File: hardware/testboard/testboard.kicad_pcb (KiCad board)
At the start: 2 copper layers, 175 x 140 mm, 22 parts, among them J1 Reset, P1 Conn_01x06, P2 Conn_01x06, U1 68LC040, U10 SN74ALVC164245, U11 ICE40HX4K-TQ144, U13 SST26VF023BA, U14 SN74ALVC164245, U15 SN74ALVC164245, U2 MAX232, U3 MAX232, U4 68681, U6 IS61C5128AS-25TLI, U7 IS61C5128AS-25TLI, U8 NB3N502, X1 ASE-33MHz, X2 33MHz, X3 33MHz

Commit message: simpleboard nearly complete
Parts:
- removed P1, P2: Conn_01x06, 68040:15-48-0106
- removed RN1: 4.7k, Resistor_THT:R_Array_SIP6
- added C1: 0.22uF, Capacitor_SMD:C_0603_1608Metric, F.Cu at (146.1, 60.5)
- added C10: 1uF, Capacitor_SMD:C_0805_2012Metric, F.Cu at (54.2, 145.4)
- added C11: 1uF, Capacitor_SMD:C_0805_2012Metric, F.Cu at (61.2, 137.2)
- added C12: 1uF, Capacitor_SMD:C_0805_2012Metric, F.Cu at (53.7, 149.4)
- added C13: 1uF, Capacitor_SMD:C_0805_2012Metric, F.Cu at (60.6, 143.5)
- added C14: 1uF, Capacitor_SMD:C_0805_2012Metric, F.Cu at (54.2, 142.9)
- added C15: 15pF, Capacitor_SMD:C_0603_1608Metric, F.Cu at (62.9, 101.6)
- added C16: 15pF, Capacitor_SMD:C_0603_1608Metric, F.Cu at (62.9, 99.1)
- added C17: C_Polarized_Small_US, Capacitor_THT:CP_Radial_D5.0mm_P2.00mm, F.Cu at (78.7, 117.4)
- added C18: 100nF, Capacitor_SMD:C_0603_1608Metric, F.Cu at (56.8, 77.5)
- added C19: 100nF, Capacitor_SMD:C_0603_1608Metric, F.Cu at (132.4, 57.1)
- added C2: 22uF, Capacitor_THT:CP_Radial_D5.0mm_P2.00mm, F.Cu at (143.5, 81.3)
- added C21: 100nF, Capacitor_SMD:C_0603_1608Metric, F.Cu at (160.5, 114.3)
- added C22: 100nF, Capacitor_SMD:C_0603_1608Metric, F.Cu at (180.1, 114.3)
- added C23: 100nF, Capacitor_SMD:C_0603_1608Metric, F.Cu at (116.2, 46.4)
- added C24: 100nF, Capacitor_SMD:C_0603_1608Metric, F.Cu at (124.6, 47.7)
- added C25: 1uF, Capacitor_SMD:C_0805_2012Metric, F.Cu at (72.5, 137.9)
- added C26: 1uF, Capacitor_SMD:C_0805_2012Metric, F.Cu at (42.0, 148.9)
- added C27: 100nF, Capacitor_SMD:C_0603_1608Metric, F.Cu at (134.6, 131.3)
- added C28: 220uF, Capacitor_THT:CP_Radial_D8.0mm_P2.50mm, F.Cu at (43.2, 45.8)
- added C3: 220pF, Capacitor_SMD:C_0603_1608Metric, F.Cu at (183.7, 90.2)
- added C30: 100nF, Capacitor_SMD:C_0603_1608Metric, F.Cu at (100.2, 54.8)
- added C31: 100nF, Capacitor_SMD:C_0603_1608Metric, F.Cu at (85.8, 52.5)
- added C32: 100nF, Capacitor_SMD:C_0603_1608Metric, B.Cu at (122.3, 83.0)
- added C33: 100nF, Capacitor_SMD:C_0603_1608Metric, B.Cu at (122.3, 77.9)
- added C34: 100nF, Capacitor_SMD:C_0603_1608Metric, B.Cu at (116.3, 83.0)
- added C35: 100nF, Capacitor_SMD:C_0603_1608Metric, B.Cu at (116.3, 77.9)
- added C36: 100nF, Capacitor_SMD:C_0603_1608Metric, B.Cu at (75.6, 71.0)
- added C37: 100nF, Capacitor_SMD:C_0603_1608Metric, B.Cu at (75.6, 76.1)
- added C38: 100nF, Capacitor_SMD:C_0603_1608Metric, B.Cu at (69.5, 76.1)
- added C39: 100nF, Capacitor_SMD:C_0603_1608Metric, B.Cu at (69.5, 71.0)
- added C4: 0.22uF, Capacitor_SMD:C_0603_1608Metric, F.Cu at (196.8, 83.8)
- added C40: 100nF, Capacitor_SMD:C_0603_1608Metric, B.Cu at (101.4, 100.1)
- added C41: 100nF, Capacitor_SMD:C_0603_1608Metric, B.Cu at (80.0, 94.8)
- added C42: 100nF, Capacitor_SMD:C_0603_1608Metric, B.Cu at (86.4, 94.8)
- added C43: 100nF, Capacitor_SMD:C_0603_1608Metric, B.Cu at (106.4, 100.1)
- added C44: 100nF, Capacitor_SMD:C_0603_1608Metric, B.Cu at (101.4, 95.3)
- added C45: 100nF, Capacitor_SMD:C_0603_1608Metric, B.Cu at (80.0, 100.8)
- added C46: 100nF, Capacitor_SMD:C_0603_1608Metric, B.Cu at (106.4, 95.3)
- added C47: 100nF, Capacitor_SMD:C_0603_1608Metric, B.Cu at (86.4, 100.8)
- added C48: 100nF, Capacitor_SMD:C_0603_1608Metric, F.Cu at (83.6, 75.2)
- added C49: 100nF, Capacitor_SMD:C_0603_1608Metric, F.Cu at (110.4, 83.1)
- added C5: 22uF, Capacitor_THT:CP_Radial_D5.0mm_P2.00mm, F.Cu at (143.5, 48.3)
- added C50: 100nF, Capacitor_SMD:C_0603_1608Metric, F.Cu at (91.5, 90.4)
- added C51: 100nF, Capacitor_SMD:C_0603_1608Metric, B.Cu at (116.6, 100.1)
- added C52: 100nF, Capacitor_SMD:C_0603_1608Metric, B.Cu at (121.7, 100.1)
- added C53: 100nF, Capacitor_SMD:C_0603_1608Metric, B.Cu at (121.7, 95.3)
- added C54: 100nF, Capacitor_SMD:C_0603_1608Metric, B.Cu at (116.6, 95.3)
- added C55: 100nF, Capacitor_SMD:C_0603_1608Metric, F.Cu at (99.4, 63.3)
- added C56: 4.7uF, Capacitor_SMD:C_0603_1608Metric, F.Cu at (94.0, 90.7)
- added C57: 4.7uF, Capacitor_SMD:C_0603_1608Metric, F.Cu at (82.7, 78.1)
- added C58: 4.7uF, Capacitor_SMD:C_0603_1608Metric, F.Cu at (109.4, 86.4)
- added C59: 4.7uF, Capacitor_SMD:C_0603_1608Metric, F.Cu at (98.3, 61.6)
- added C6: 220pF, Capacitor_SMD:C_0603_1608Metric, F.Cu at (196.8, 44.0)
- added C60: 4.7uF, Capacitor_SMD:C_0603_1608Metric, F.Cu at (83.8, 65.4)
- added C61: 100nF, Capacitor_SMD:C_0603_1608Metric, F.Cu at (83.8, 63.5)
- added C62: 100nF, Capacitor_SMD:C_0603_1608Metric, F.Cu at (119.2, 67.0)
- added C63: 100nF, Capacitor_SMD:C_0603_1608Metric, F.Cu at (111.7, 58.4)
- added C64: 4.7uF, Capacitor_SMD:C_0603_1608Metric, F.Cu at (69.8, 57.9)
- added C65: 4.7uF, Capacitor_SMD:C_0603_1608Metric, F.Cu at (77.5, 57.9)
- added C66: 4.7uF, Capacitor_SMD:C_0603_1608Metric, B.Cu at (108.8, 70.1)
- added C67: 4.7uF, Capacitor_SMD:C_0603_1608Metric, B.Cu at (101.5, 70.1)
- added C68: 100nF, Capacitor_SMD:C_0603_1608Metric, B.Cu at (102.2, 73.8)
- added C69: 4.7uF, Capacitor_SMD:C_0603_1608Metric, B.Cu at (104.1, 75.1)
- added C7: 1uF, Capacitor_SMD:C_0805_2012Metric, F.Cu at (58.4, 138.1)
- added C70: 100nF, Capacitor_SMD:C_0603_1608Metric, B.Cu at (94.8, 68.6)
- added C71: 100nF, Capacitor_SMD:C_0603_1608Metric, B.Cu at (98.3, 83.2)
- added C72: 4.7uF, Capacitor_SMD:C_0603_1608Metric, B.Cu at (94.0, 75.7)
- added C73: 100nF, Capacitor_SMD:C_0603_1608Metric, F.Cu at (53.3, 36.3)
- added C74: 100nF, Capacitor_SMD:C_0603_1608Metric, F.Cu at (60.5, 57.1)
- added C75: 100nF, Capacitor_SMD:C_0603_1608Metric, F.Cu at (53.8, 57.1)
- added C8: 1uF, Capacitor_SMD:C_0805_2012Metric, F.Cu at (60.6, 141.0)
- added C9: 1uF, Capacitor_SMD:C_0805_2012Metric, F.Cu at (56.3, 148.4)
- added D1: LTST-C191KGKT, LED_SMD:LED_0603_1608Metric, F.Cu at (99.1, 41.4)
- added D2: D_Schottky, Diode_SMD:D_0603_1608Metric, F.Cu at (76.1, 41.4)
- added D3: LED, LED_THT:LED_D3.0mm, F.Cu at (32.5, 78.7)
- added FB1: FerriteBead, Inductor_SMD:L_0805_2012Metric_Pad1.15x1.40mm_HandSolder, F.Cu at (152.4, 37.1)
- added J2: Conn_01x06, Connector_JST:JST_PH_B6B-PH-K_1x06_P2.00mm_Vertical, F.Cu at (88.7, 35.6)
- added R1: 4.7k, Resistor_SMD:R_0603_1608Metric, F.Cu at (185.4, 37.3)
- added R10: 100, Resistor_SMD:R_0603_1608Metric, B.Cu at (94.8, 83.8)
- added R11: 4.7k, Resistor_SMD:R_0603_1608Metric, F.Cu at (180.3, 37.3)
- added R12: 4.7k, Resistor_SMD:R_0603_1608Metric, F.Cu at (177.8, 37.3)
- added R13: 4.7k, Resistor_SMD:R_0603_1608Metric, F.Cu at (175.3, 37.3)
- added R14: 10k, Resistor_SMD:R_0603_1608Metric, F.Cu at (94.2, 57.8)
- added R15: 2.2K, Resistor_SMD:R_0603_1608Metric, F.Cu at (38.7, 75.4)
- added R16: 2.2K, Resistor_SMD:R_0603_1608Metric, F.Cu at (100.3, 42.3)
- added R17: 10K, Resistor_SMD:R_0603_1608Metric, F.Cu at (81.1, 51.4)
- added R18: 10K, Resistor_SMD:R_0603_1608Metric, F.Cu at (89.6, 52.8)
- added R19: 10k, Resistor_SMD:R_0603_1608Metric, F.Cu at (94.2, 59.7)
- added R2: 1k, Resistor_SMD:R_0603_1608Metric, F.Cu at (62.2, 130.5)
- added R20: R_Small_US, Resistor_SMD:R_0603_1608Metric, F.Cu at (81.3, 85.5)
- added R21: 1k, Resistor_SMD:R_0603_1608Metric, F.Cu at (94.0, 121.9)
- added R22: 1k, Resistor_SMD:R_0603_1608Metric, F.Cu at (94.0, 120.7)
- added R23: 1k, Resistor_SMD:R_0603_1608Metric, F.Cu at (40.6, 67.8)
- added R24: 1k, Resistor_SMD:R_0603_1608Metric, F.Cu at (58.0, 47.0)
- added R25: 1k, Resistor_SMD:R_0603_1608Metric, F.Cu at (40.6, 59.2)
- added R26: 4.7k, Resistor_SMD:R_0603_1608Metric, F.Cu at (188.0, 37.3)
- added R27: 4.7k, Resistor_SMD:R_0603_1608Metric, F.Cu at (149.9, 37.3)
- added R28: 4.7k, Resistor_SMD:R_0603_1608Metric, F.Cu at (182.9, 37.3)
- added R29: 4.7k, Resistor_SMD:R_0603_1608Metric, F.Cu at (172.7, 37.3)
- added R3: 4.7k, Resistor_SMD:R_0603_1608Metric, F.Cu at (167.6, 37.3)
- added R4: 4.7k, Resistor_SMD:R_0603_1608Metric, F.Cu at (170.2, 37.3)
- added R5: 4.7k, Resistor_SMD:R_0603_1608Metric, F.Cu at (165.1, 37.3)
- added R6: 4.7k, Resistor_SMD:R_0603_1608Metric, F.Cu at (162.6, 37.3)
- added R7: 4.7k, Resistor_SMD:R_0603_1608Metric, F.Cu at (160.0, 37.3)
- added R8: 4.7k, Resistor_SMD:R_0603_1608Metric, F.Cu at (154.9, 37.3)
- added R9: 4.7k, Resistor_SMD:R_0603_1608Metric, F.Cu at (157.5, 37.3)
- added RN2: 1k, Resistor_THT:R_Array_SIP10, F.Cu at (141.0, 76.2)
- added SW1: Button, Button_Switch_THT:SW_PUSH_6mm, F.Cu at (30.5, 70.0)
- added SW2: Button, Button_Switch_THT:SW_PUSH_6mm, F.Cu at (30.5, 57.3)
- added U12: 74AHCT04, Package_SO:TSSOP-14_4.4x5mm_P0.65mm, F.Cu at (104.0, 55.4)
- added U16: SN74ALVC164245, Package_SO:TSSOP-48_6.1x12.5mm_P0.5mm, F.Cu at (83.2, 97.9)
- added U17: SN74ALVC164245, Package_SO:TSSOP-48_6.1x12.5mm_P0.5mm, F.Cu at (103.8, 97.7)
- added U18: SN74LVC07, Package_SO:TSSOP-14_4.4x5mm_P0.65mm, F.Cu at (115.4, 67.4)
- added U19: SN74LVC07, Package_SO:TSSOP-14_4.4x5mm_P0.65mm, F.Cu at (115.4, 58.5)
- added U20: AP2112K-3.3, Package_TO_SOT_SMD:SOT-23-5, F.Cu at (73.8, 58.1)
- added U21: AP2112K-1.2, Package_TO_SOT_SMD:SOT-23-5, B.Cu at (105.2, 70.2)
- added U22: 74LVC1G08, Package_TO_SOT_SMD:SOT-23-5, F.Cu at (56.8, 37.0)
- added U23: TL7705A, Package_SO:SOIC-8_3.9x4.9mm_P1.27mm, F.Cu at (57.8, 52.1)
- added U5: 74LVC1G04, Package_TO_SOT_SMD:SOT-23-5, F.Cu at (132.1, 61.0)
- added Y1: 3.6864MHz, Crystal:Crystal_C38-LF_D3.0mm_L8.0mm_Vertical, F.Cu at (67.5, 101.2)
- J1: value Reset -> Barrel_Jack; footprint Connector_PinHeader_2.54mm:PinHeader_1x02_P2.54mm_Vertical -> Connector_BarrelJack:BarrelJack_GCT_DCJ200-10-A_Horizontal
- U9: footprint Package_LCC:PLCC-68_SMD-Socket -> Package_LCC:PLCC-68_THT-Socket
- moved X2 87.6 mm to (111.8, 41.4), turned to 0 degrees
- moved X1 81.9 mm to (123.4, 37.1), turned to 0 degrees
- moved X3 80.4 mm to (119.4, 41.4), turned to 0 degrees
- moved U1 74.7 mm to (193.0, 86.4), turned to 180 degrees
- moved U4 68.7 mm to (43.2, 81.3), turned to 0 degrees
- moved U10 67.4 mm to (119.0, 97.3), turned to 90 degrees
- moved U7 67.1 mm to (180.6, 126.4), turned to 0 degrees
- moved U8 64.6 mm to (130.3, 47.2), turned to 0 degrees
- moved U15 59.0 mm to (72.5, 72.9), turned to 0 degrees
- moved U2 45.8 mm to (66.6, 141.6), turned to 0 degrees
- moved U9 41.0 mm to (127.0, 132.1), turned to -90 degrees
- moved J1 38.2 mm to (36.8, 37.5), turned to -90 degrees
- moved U6 36.1 mm to (160.5, 126.4), turned to 0 degrees
- moved U13 26.2 mm to (86.2, 56.9), turned to 0 degrees
- moved U11 24.7 mm to (96.3, 76.1), turned to 180 degrees
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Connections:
- J1 pad 1: unconnected-(J1-Pin_1-Pad1) -> +5V
- U1 pad R16: /~{TS} -> Net-(U1A-~{TS})
- U1 pad R3: /CPU/~{SW_RST} -> /~{SW_RST}
- U1 pad S11: /~{TCI}/~{TBI} -> /~{TBI}
- U1 pad S7: /CPU/~{HW_RST} -> /~{RST}
- U1 pad T10: /~{TCI}/~{TBI} -> /~{TCI}
- U10 pad 1: /FPGA/FPGA_D_DIR -> GND
- U10 pad 11: /PD30 -> GND
- U10 pad 12: /PD31 -> GND
- U10 pad 13: /PA0 -> /SIZ0
- U10 pad 14: /PA1 -> /SIZ1
- U10 pad 16: unconnected-(U10A-2B3-Pad16) -> /~{COM_IRQ}
- U10 pad 17: unconnected-(U10A-2B4-Pad17) -> /~{RST}
- U10 pad 19: unconnected-(U10A-2B5-Pad19) -> /~{TS}
- U10 pad 2: /PD24 -> /TT0
- U10 pad 20: unconnected-(U10A-2B6-Pad20) -> /~{TIP}
- U10 pad 22: /FPGA/~{68150_DS} -> /~{DS}
- U10 pad 23: unconnected-(U10A-2B8-Pad23) -> /R/~{W}
- U10 pad 26: unconnected-(U10A-2A8-Pad26) -> /FPGA/LV_R/~{W}
- U10 pad 29: unconnected-(U10A-2A6-Pad29) -> /FPGA/LV_~{TIP}
- U10 pad 3: /PD25 -> /TT1
- U10 pad 30: unconnected-(U10A-2A5-Pad30) -> /FPGA/LV_~{TS}
- U10 pad 32: unconnected-(U10A-2A4-Pad32) -> /FPGA/LV_~{RST}
- U10 pad 33: unconnected-(U10A-2A3-Pad33) -> /FPGA/LV_~{COM_IRQ}
- U10 pad 35: /FPGA/LV_PA1 -> /FPGA/LV_SIZ1
- U10 pad 36: /FPGA/LV_PA0 -> /FPGA/LV_SIZ0
- U10 pad 37: /FPGA/FPGA_D7 -> unconnected-(U10A-1A8-Pad37)
- U10 pad 38: /FPGA/FPGA_D6 -> unconnected-(U10A-1A7-Pad38)
- U10 pad 40: /FPGA/FPGA_D5 -> unconnected-(U10A-1A6-Pad40)
- U10 pad 41: /FPGA/FPGA_D4 -> /FPGA/LV_TM2
- U10 pad 43: /FPGA/FPGA_D3 -> /FPGA/LV_TM1
- U10 pad 44: /FPGA/FPGA_D2 -> /FPGA/LV_TM0
- U10 pad 46: /FPGA/FPGA_D1 -> /FPGA/LV_TT1
- U10 pad 47: /FPGA/FPGA_D0 -> /FPGA/LV_TT0
- U10 pad 48: /FPGA/FPGA_D_~{OE} -> GND
- U10 pad 5: /PD26 -> /TM0
- U10 pad 6: /PD27 -> /TM1
- U10 pad 8: /PD28 -> /TM2
- U10 pad 9: /PD29 -> GND
- U11 pad 1: /FPGA/~{DSACK0} -> /FPGA/LV.A0
- U11 pad 10: unconnected-(U11D-IOL_5B-Pad10) -> /FPGA/LV.A7
- U11 pad 101: /FPGA/LV.A23 -> /FPGA/LV_D7
- U11 pad 102: /FPGA/LV.A24 -> /FPGA/LV_D8
- U11 pad 104: /FPGA/LV.A25 -> /FPGA/LV_D9
- U11 pad 105: /FPGA/LV.A26 -> /FPGA/LV_D10
- U11 pad 106: /FPGA/LV.A27 -> /FPGA/LV_D11
- U11 pad 107: /FPGA/LV.A28 -> /FPGA/LV_D12
- U11 pad 109: +3.3V -> unconnected-(U11E-VPP_FAST-Pad109)
- U11 pad 11: unconnected-(U11D-IOL_8A-Pad11) -> /FPGA/LV.A8
- U11 pad 110: /FPGA/LV.A29 -> /FPGA/LV_D13
- U11 pad 111: +3.3V -> +1V2
- U11 pad 112: /FPGA/LV.A30 -> /FPGA/LV_D14
- U11 pad 113: /FPGA/LV.A31 -> /FPGA/LV_D15
- U11 pad 114: /FPGA/FPGA_D0 -> /FPGA/LV_D16
- U11 pad 115: /FPGA/FPGA_D1 -> /FPGA/LV_D17
- U11 pad 116: /FPGA/FPGA_D2 -> /FPGA/LV_D18
- U11 pad 117: /FPGA/FPGA_D3 -> /FPGA/LV_D19
- U11 pad 118: /FPGA/FPGA_D4 -> /FPGA/LV_D20
- U11 pad 119: /FPGA/FPGA_D5 -> /FPGA/LV_D21
- U11 pad 12: unconnected-(U11D-IOL_8B-Pad12) -> /FPGA/LV.A9
- U11 pad 120: /FPGA/FPGA_D6 -> /FPGA/LV_D22
- U11 pad 121: /FPGA/FPGA_D7 -> /FPGA/LV_D23
- U11 pad 122: unconnected-(U11A-IOT_190-Pad122) -> /FPGA/LV_D24
- U11 pad 124: unconnected-(U11A-IOT_191-Pad124) -> /FPGA/LV_D25
- U11 pad 125: unconnected-(U11A-IOT_192-Pad125) -> /FPGA/LV_D26
- U11 pad 126: +3.3V -> /FPGA/VCC_PLL
- U11 pad 127: GND -> /FPGA/GND_PLL
- U11 pad 128: unconnected-(U11A-IOT_197_GBIN1-Pad128) -> /FPGA/LV_D27
- U11 pad 129: unconnected-(U11A-IOT_198_GBIN0-Pad129) -> /FPGA/LV_D28
- U11 pad 130: unconnected-(U11A-IOT_206-Pad130) -> /FPGA/LV_D29
- U11 pad 134: unconnected-(U11A-IOT_212-Pad134) -> /FPGA/LV_D30
- U11 pad 135: unconnected-(U11A-IOT_213-Pad135) -> /FPGA/LV_D31
- U11 pad 136: unconnected-(U11A-IOT_214-Pad136) -> /FPGA/LV_TT0
- U11 pad 137: unconnected-(U11A-IOT_215-Pad137) -> /FPGA/LV_TT1
- U11 pad 138: unconnected-(U11A-IOT_216-Pad138) -> /FPGA/LV_SIZ0
- U11 pad 139: unconnected-(U11A-IOT_217-Pad139) -> /FPGA/LV_SIZ1
- U11 pad 141: unconnected-(U11A-IOT_219-Pad141) -> /FPGA/LV_~{TS}
- U11 pad 142: unconnected-(U11A-IOT_220-Pad142) -> /FPGA/LV_~{TIP}
- U11 pad 143: unconnected-(U11A-IOT_221-Pad143) -> /FPGA/LV_~{68150_DS}
- U11 pad 144: unconnected-(U11A-IOT_222-Pad144) -> /FPGA/LV_R/~{W}
- U11 pad 15: unconnected-(U11D-IOL_10A-Pad15) -> /FPGA/LV.A10
- U11 pad 16: unconnected-(U11D-IOL_10B-Pad16) -> /FPGA/LV.A11
- U11 pad 17: unconnected-(U11D-IOL_12A-Pad17) -> /FPGA/LV.A12
- U11 pad 18: unconnected-(U11D-IOL_12B-Pad18) -> /FPGA/LV.A13
- U11 pad 19: unconnected-(U11D-IOL_13A-Pad19) -> /FPGA/LV.A14
- U11 pad 2: /FPGA/~{DSACK1} -> /FPGA/LV.A1
- U11 pad 20: unconnected-(U11D-IOL_13B_GBIN7-Pad20) -> /FPGA/LV.A15
- U11 pad 21: unconnected-(U11D-IOL_14A_GBIN6-Pad21) -> /FPGA/LV_~{DSACK0}
- U11 pad 22: unconnected-(U11D-IOL_14B-Pad22) -> /FPGA/LV_~{DSACK1}
- U11 pad 23: unconnected-(U11D-IOL_17A-Pad23) -> /FPGA/LV_TM0
- U11 pad 24: unconnected-(U11D-IOL_17B-Pad24) -> /FPGA/LV_TM1
- U11 pad 25: unconnected-(U11D-IOL_18A-Pad25) -> /FPGA/LV_TM2
- U11 pad 26: unconnected-(U11D-IOL_18B-Pad26) -> /FPGA/LV_~{TA}
- U11 pad 27: +3.3V -> +1V2
- U11 pad 28: unconnected-(U11D-IOL_23A-Pad28) -> /FPGA/LV_~{TEA}
- U11 pad 29: unconnected-(U11D-IOL_23B-Pad29) -> /FPGA/LV_~{TBI}
- U11 pad 3: unconnected-(U11D-IOL_3A-Pad3) -> /FPGA/LV.A2
- U11 pad 31: unconnected-(U11D-IOL_24A-Pad31) -> /FPGA/LV_~{TCI}
- U11 pad 32: unconnected-(U11D-IOL_24B-Pad32) -> /FPGA/LV_~{IPL0}
- U11 pad 33: unconnected-(U11D-IOL_25A-Pad33) -> /FPGA/LV_~{IPL1}
- U11 pad 34: unconnected-(U11D-IOL_25B-Pad34) -> /FPGA/LV_~{IPL2}
- U11 pad 4: unconnected-(U11D-IOL_3B-Pad4) -> /FPGA/LV.A3
- U11 pad 40: +3.3V -> +1V2
- U11 pad 41: unconnected-(U11C-IOB_63-Pad41) -> /FPGA/LV_RAM_CS
- U11 pad 42: unconnected-(U11C-IOB_64-Pad42) -> /FPGA/LV_COM_IACK
- U11 pad 43: unconnected-(U11C-IOB_71-Pad43) -> /FPGA/LV_~{COM_IRQ}
- U11 pad 44: unconnected-(U11C-IOB_72-Pad44) -> /FPGA/LV_COM_CS
- U11 pad 45: unconnected-(U11C-IOB_73-Pad45) -> /FPGA/LV_68150_CS
- U11 pad 47: unconnected-(U11C-IOB_79-Pad47) -> /FPGA/FPGA_D_~{OE}
- U11 pad 48: unconnected-(U11C-IOB_80-Pad48) -> /FPGA/FPGA_D_DIR
- U11 pad 49: unconnected-(U11C-IOB_81_GBIN5-Pad49) -> /FPGA/LV_~{RST}
- U11 pad 53: GND -> /FPGA/GND_PLL
- U11 pad 54: +3.3V -> /FPGA/VCC_PLL
- U11 pad 55: /FPGA/FPGA_A_DIR -> /FPGA/FPGA_LED
- U11 pad 56: /FPGA/FPGA_A_~{OE} -> /FPGA/FPGA_BTN
- U11 pad 66: unconnected-(U11E-~{CRESET}-Pad66) -> Net-(U11E-~{CRESET})
- U11 pad 7: unconnected-(U11D-IOL_4A-Pad7) -> /FPGA/LV.A4
- U11 pad 73: /FPGA/LV.A0 -> /FPGA/LV.A16
- U11 pad 74: /FPGA/LV.A1 -> /FPGA/LV.A17
- U11 pad 75: /FPGA/LV.A2 -> /FPGA/LV.A18
- U11 pad 76: /FPGA/LV.A3 -> /FPGA/LV.A19
- U11 pad 78: /FPGA/LV.A4 -> /FPGA/LV.A20
- U11 pad 79: /FPGA/LV.A5 -> /FPGA/LV.A21
- U11 pad 8: unconnected-(U11D-IOL_4B-Pad8) -> /FPGA/LV.A5
- U11 pad 80: /FPGA/LV.A6 -> /FPGA/LV.A22
- U11 pad 81: /FPGA/LV.A7 -> /FPGA/LV.A23
- U11 pad 82: /FPGA/LV.A8 -> /FPGA/LV.A24
- U11 pad 83: /FPGA/LV.A9 -> /FPGA/LV.A25
- U11 pad 84: /FPGA/LV.A10 -> /FPGA/LV.A26
- U11 pad 85: /FPGA/LV.A11 -> /FPGA/LV.A27
- U11 pad 87: /FPGA/LV.A12 -> /FPGA/LV.A28
- U11 pad 88: /FPGA/LV.A13 -> /FPGA/LV.A29
- U11 pad 9: unconnected-(U11D-IOL_5A-Pad9) -> /FPGA/LV.A6
- U11 pad 90: /FPGA/LV.A14 -> /FPGA/LV.A30
- U11 pad 91: /FPGA/LV.A15 -> /FPGA/LV.A31
- U11 pad 92: +3.3V -> +1V2
- U11 pad 93: /FPGA/LV.A16 -> /FPGA/LV_D0
- U11 pad 94: /FPGA/LV.A17 -> /FPGA/LV_D1
- U11 pad 95: /FPGA/LV.A18 -> /FPGA/LV_D2
- U11 pad 96: /FPGA/LV.A19 -> /FPGA/LV_D3
- U11 pad 97: /FPGA/LV.A20 -> /FPGA/LV_D4
- U11 pad 98: /FPGA/LV.A21 -> /FPGA/LV_D5
- U11 pad 99: /FPGA/LV.A22 -> /FPGA/LV_D6
- U14 pad 1: /FPGA/FPGA_A_DIR -> GND
- U14 pad 24: /FPGA/FPGA_A_DIR -> GND
- U14 pad 25: /FPGA/FPGA_A_~{OE} -> GND
- U14 pad 48: /FPGA/FPGA_A_~{OE} -> GND
- U15 pad 1: /FPGA/FPGA_A_DIR -> GND
- U15 pad 24: /FPGA/FPGA_A_DIR -> GND
- U15 pad 25: /FPGA/FPGA_A_~{OE} -> GND
- U15 pad 48: /FPGA/FPGA_A_~{OE} -> GND
- U4 pad 34: /IO/~{RESET} -> /~{RST}
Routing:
- net /~{RST}: track 0.00 -> 265.3 mm, vias 0 -> 4
- net /A18: track 0.00 -> 261.0 mm, vias 0 -> 2
- net /A17: track 0.00 -> 251.9 mm, vias 0 -> 3
- net /A16: track 0.00 -> 236.9 mm, vias 0 -> 4
- net /A2: track 0.00 -> 231.4 mm, vias 0 -> 5
- net /A3: track 0.00 -> 227.9 mm, vias 0 -> 5
- net /A19: track 0.00 -> 212.1 mm, vias 0 -> 3
- net /A26: track 0.00 -> 188.9 mm, vias 0 -> 4
- net /A23: track 0.00 -> 187.5 mm, vias 0 -> 3
- net /A11: track 0.00 -> 186.4 mm, vias 0 -> 1
- net /A27: track 0.00 -> 183.6 mm, vias 0 -> 1
- net /A31: track 0.00 -> 181.3 mm, vias 0 -> 4
- net /A13: track 0.00 -> 180.6 mm, vias 0 -> 2
- net /A10: track 0.00 -> 179.9 mm, vias 0 -> 3
- net /A21: track 0.00 -> 179.8 mm, vias 0 -> 2
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- added copper zone on In2.Cu, net +3.3V
- added copper zone on In2.Cu, net +5V
- added copper zone on In1.Cu, net GND
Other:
- board size 175 x 140 mm -> 180.3 x 132.1 mm
- copper layers 2 -> 4

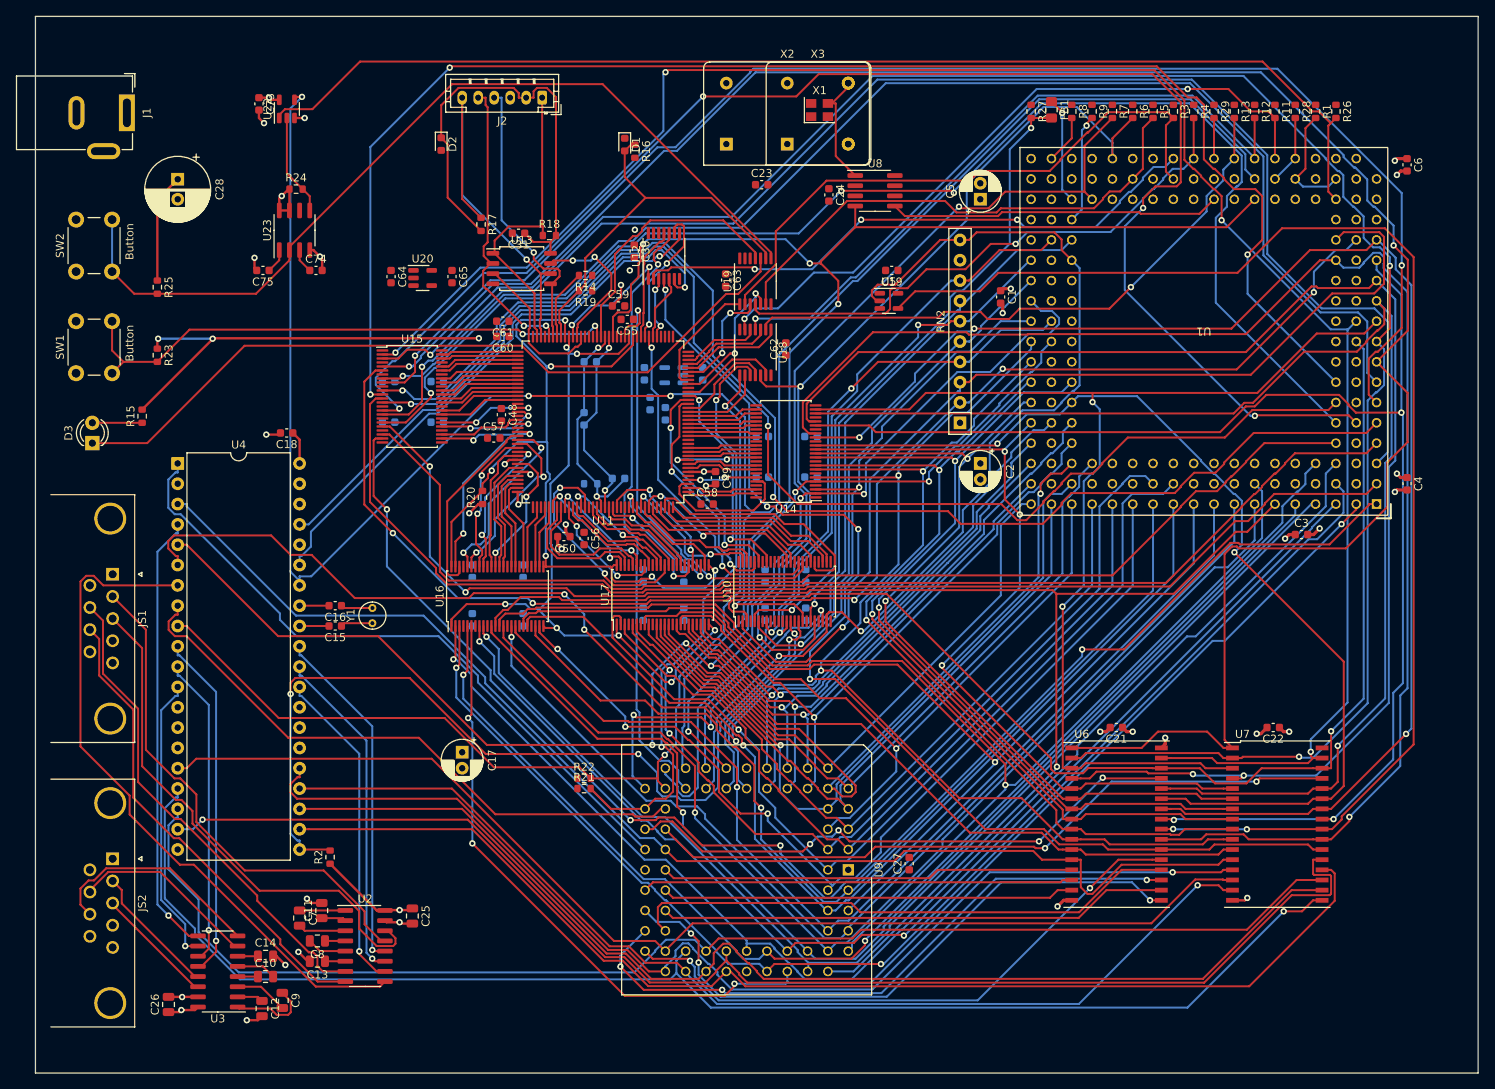
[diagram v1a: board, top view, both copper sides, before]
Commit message: fix up FPGA pinning
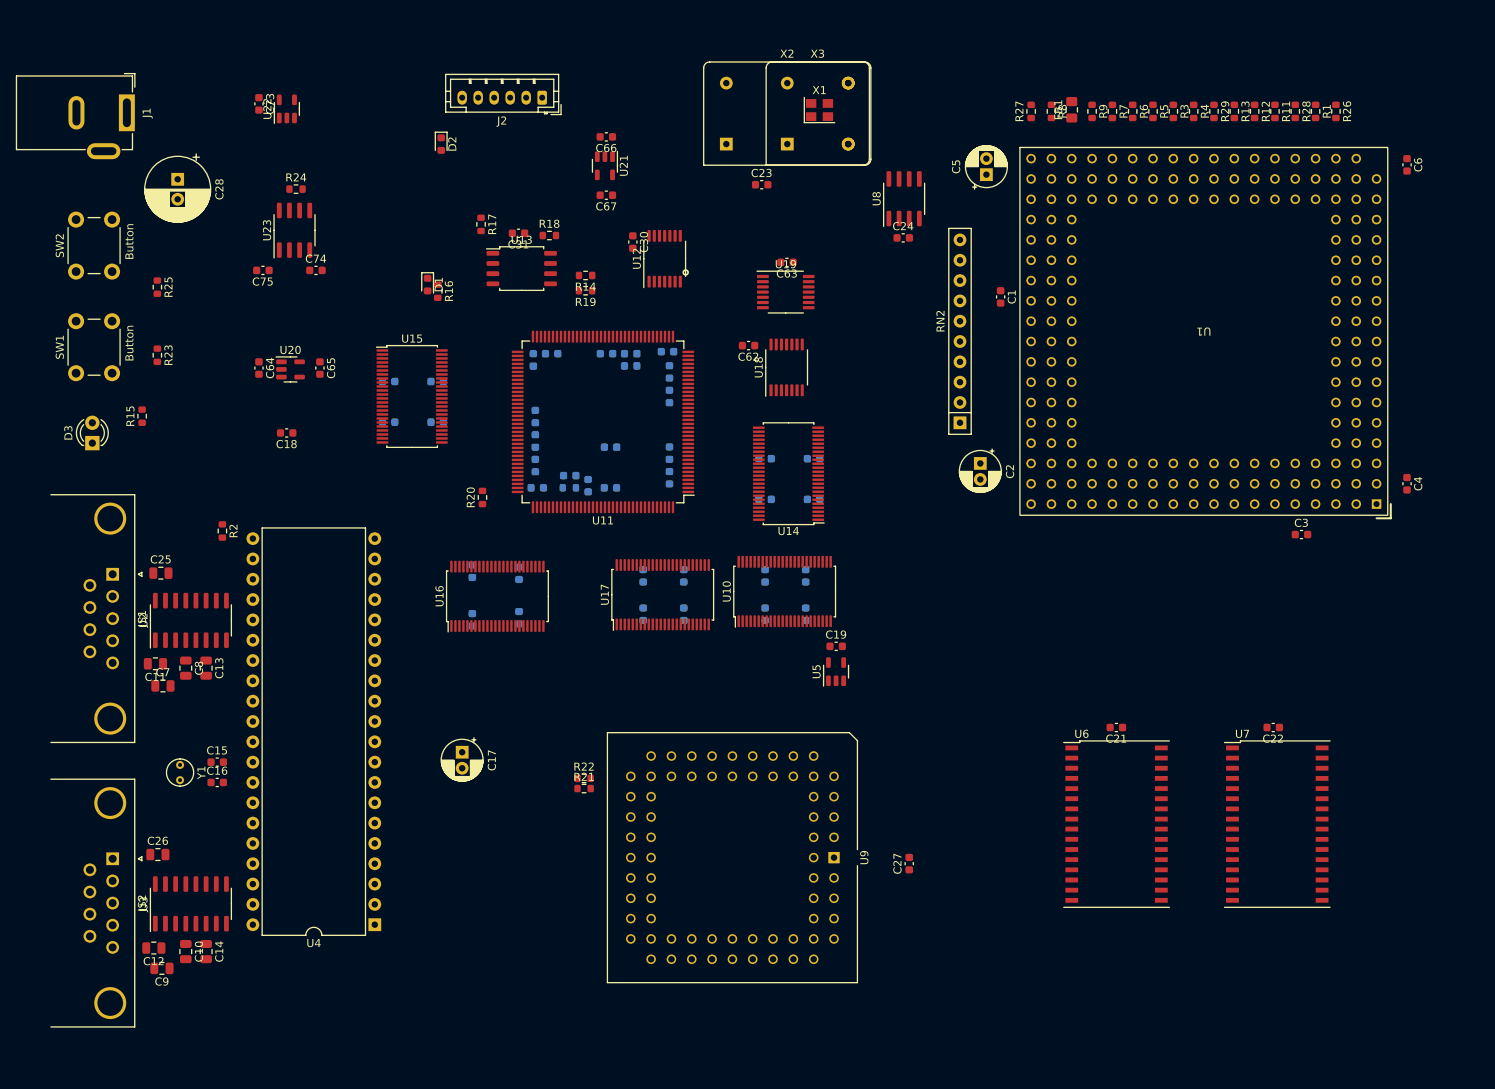
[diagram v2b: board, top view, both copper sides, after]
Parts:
- added C20: 100nF, Capacitor_SMD:C_0603_1608Metric, B.Cu at (88.1, 84.3)
- added C29: 100nF, Capacitor_SMD:C_0603_1608Metric, B.Cu at (87.9, 75.4)
- added C76: 100nF, Capacitor_SMD:C_0603_1608Metric, B.Cu at (104.4, 67.3)
- C48, C49, C50, C55, C56, C57, C58, C59, C60, C61: moved to B.Cu
- C66, C67, U21: moved to F.Cu
- moved U4 62.7 mm to (67.8, 138.9), turned to 180 degrees
- moved C25 53.1 mm to (41.1, 95.0), turned to 0 degrees
- moved C19 47.5 mm to (125.5, 104.1), turned to 0 degrees
- moved U5 46.8 mm to (125.5, 107.3), turned to 90 degrees
- moved U2 46.2 mm to (44.8, 100.9), turned to 90 degrees
- moved R2 42.9 mm to (48.8, 89.7), turned to -90 degrees
- moved C13 39.2 mm to (46.7, 106.9), turned to -90 degrees
- moved C8 37.9 mm to (44.2, 106.9), turned to -90 degrees
- moved C11 37.2 mm to (40.4, 106.3), turned to 180 degrees
- moved C7 33.7 mm to (41.3, 109.1), turned to 0 degrees
- moved C66 32.0 mm to (96.8, 40.5), turned to 180 degrees
- moved R16 30.2 mm to (75.7, 59.8)
- moved D1 30.2 mm to (74.4, 58.9)
- moved Y1 29.9 mm to (43.5, 119.0), turned to -90 degrees
- moved U21 27.6 mm to (96.6, 44.1), turned to -90 degrees
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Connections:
- U11 pad 1: /FPGA/LV.A0 -> /FPGA/LV.A15
- U11 pad 10: /FPGA/LV.A7 -> /FPGA/LV.A8
- U11 pad 11: /FPGA/LV.A8 -> /FPGA/LV.A7
- U11 pad 12: /FPGA/LV.A9 -> /FPGA/LV.A6
- U11 pad 15: /FPGA/LV.A10 -> /FPGA/LV.A5
- U11 pad 16: /FPGA/LV.A11 -> /FPGA/LV.A4
- U11 pad 17: /FPGA/LV.A12 -> /FPGA/LV.A3
- U11 pad 18: /FPGA/LV.A13 -> /FPGA/LV.A2
- U11 pad 19: /FPGA/LV.A14 -> /FPGA/LV.A1
- U11 pad 2: /FPGA/LV.A1 -> /FPGA/LV.A14
- U11 pad 20: /FPGA/LV.A15 -> /FPGA/LV.A0
- U11 pad 21: /FPGA/LV_~{DSACK0} -> /BCLK
- U11 pad 22: /FPGA/LV_~{DSACK1} -> unconnected-(U11D-IOL_14B-Pad22)
- U11 pad 26: /FPGA/LV_~{TA} -> unconnected-(U11D-IOL_18B-Pad26)
- U11 pad 28: /FPGA/LV_~{TEA} -> /FPGA/LV_~{IPL0}
- U11 pad 29: /FPGA/LV_~{TBI} -> /FPGA/LV_~{IPL1}
- U11 pad 3: /FPGA/LV.A2 -> /FPGA/LV.A13
- U11 pad 31: /FPGA/LV_~{TCI} -> /FPGA/LV_~{IPL2}
- U11 pad 32: /FPGA/LV_~{IPL0} -> /FPGA/LV_~{DSACK0}
- U11 pad 33: /FPGA/LV_~{IPL1} -> /FPGA/LV_~{DSACK1}
- U11 pad 34: /FPGA/LV_~{IPL2} -> /FPGA/LV_~{TA}
- U11 pad 37: unconnected-(U11C-IOB_56-Pad37) -> /FPGA/LV_~{TEA}
- U11 pad 38: unconnected-(U11C-IOB_57-Pad38) -> /FPGA/LV_~{TCI}
- U11 pad 39: unconnected-(U11C-IOB_61-Pad39) -> /FPGA/LV_~{TBI}
- U11 pad 4: /FPGA/LV.A3 -> /FPGA/LV.A12
- U11 pad 41: /FPGA/LV_RAM_CS -> /FPGA/LV_COM_IACK
- U11 pad 42: /FPGA/LV_COM_IACK -> /FPGA/LV_RAM_CS
- U11 pad 43: /FPGA/LV_~{COM_IRQ} -> /FPGA/LV_AVEC
- U11 pad 52: /BCLK -> unconnected-(U11C-IOB_82_GBIN4-Pad52)
- U11 pad 62: /FPGA/LV_AVEC -> unconnected-(U11C-IOB_102-Pad62)
- U11 pad 7: /FPGA/LV.A4 -> /FPGA/LV.A11
- U11 pad 8: /FPGA/LV.A5 -> /FPGA/LV.A10
- U11 pad 9: /FPGA/LV.A6 -> /FPGA/LV.A9
- U14 pad 11: /A6 -> /A9
- U14 pad 12: /A7 -> /A8
- U14 pad 13: /A8 -> /A7
- U14 pad 14: /A9 -> /A6
- U14 pad 16: /A10 -> /A5
- U14 pad 17: /A11 -> /A4
- U14 pad 19: /A12 -> /A3
- U14 pad 2: /A0 -> /A15
- U14 pad 20: /A13 -> /A2
- U14 pad 22: /A14 -> /A1
- U14 pad 23: /A15 -> /A0
- U14 pad 26: /FPGA/LV.A15 -> /FPGA/LV.A0
- U14 pad 27: /FPGA/LV.A14 -> /FPGA/LV.A1
- U14 pad 29: /FPGA/LV.A13 -> /FPGA/LV.A2
- U14 pad 3: /A1 -> /A14
- U14 pad 30: /FPGA/LV.A12 -> /FPGA/LV.A3
- U14 pad 32: /FPGA/LV.A11 -> /FPGA/LV.A4
- U14 pad 33: /FPGA/LV.A10 -> /FPGA/LV.A5
- U14 pad 35: /FPGA/LV.A9 -> /FPGA/LV.A6
- U14 pad 36: /FPGA/LV.A8 -> /FPGA/LV.A7
- U14 pad 37: /FPGA/LV.A7 -> /FPGA/LV.A8
- U14 pad 38: /FPGA/LV.A6 -> /FPGA/LV.A9
- U14 pad 40: /FPGA/LV.A5 -> /FPGA/LV.A10
- U14 pad 41: /FPGA/LV.A4 -> /FPGA/LV.A11
- U14 pad 43: /FPGA/LV.A3 -> /FPGA/LV.A12
- U14 pad 44: /FPGA/LV.A2 -> /FPGA/LV.A13
- U14 pad 46: /FPGA/LV.A1 -> /FPGA/LV.A14
- U14 pad 47: /FPGA/LV.A0 -> /FPGA/LV.A15
- U14 pad 5: /A2 -> /A13
- U14 pad 6: /A3 -> /A12
- U14 pad 8: /A4 -> /A11
- U14 pad 9: /A5 -> /A10
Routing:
- net /~{RST}: track 265.3 -> 0.00 mm, vias 4 -> 0
- net /A18: track 261.0 -> 0.00 mm, vias 2 -> 0
- net /A17: track 251.9 -> 0.00 mm, vias 3 -> 0
- net /A16: track 236.9 -> 0.00 mm, vias 4 -> 0
- net /A2: track 231.4 -> 0.00 mm, vias 5 -> 0
- net /A3: track 227.9 -> 0.00 mm, vias 5 -> 0
- net /A19: track 212.1 -> 0.00 mm, vias 3 -> 0
- net /A26: track 188.9 -> 0.00 mm, vias 4 -> 0
- net /A23: track 187.5 -> 0.00 mm, vias 3 -> 0
- net /A11: track 186.4 -> 0.00 mm, vias 1 -> 0
- net /A27: track 183.6 -> 0.00 mm, vias 1 -> 0
- net /A31: track 181.3 -> 0.00 mm, vias 4 -> 0
- net /A13: track 180.6 -> 0.00 mm, vias 2 -> 0
- net /A10: track 179.9 -> 0.00 mm, vias 3 -> 0
- net /A21: track 179.8 -> 0.00 mm, vias 2 -> 0
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- removed copper zone on In2.Cu, net +3.3V
- removed copper zone on In2.Cu, net +5V
- removed copper zone on In1.Cu, net GND
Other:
- board outline removed
